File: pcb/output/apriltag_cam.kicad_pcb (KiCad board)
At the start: 4 copper layers, 48 x 48 mm, 152 parts, among them J1 USB-C, J2 JTAG, SW1 BOOTSEL, U1 LFE5U-85F-8BG381C, U10 OV9281, U11 USBLC6-2SC6, U2 RP2350A, U3 W25Q128JVSIQ, U4 TLV62569, U5 TLV62569, U6 TLV75525, U7 TLV75518, U8 TLV75528, U9 TLV75512, Y1 12MHz, Y2 24MHz 1.8V

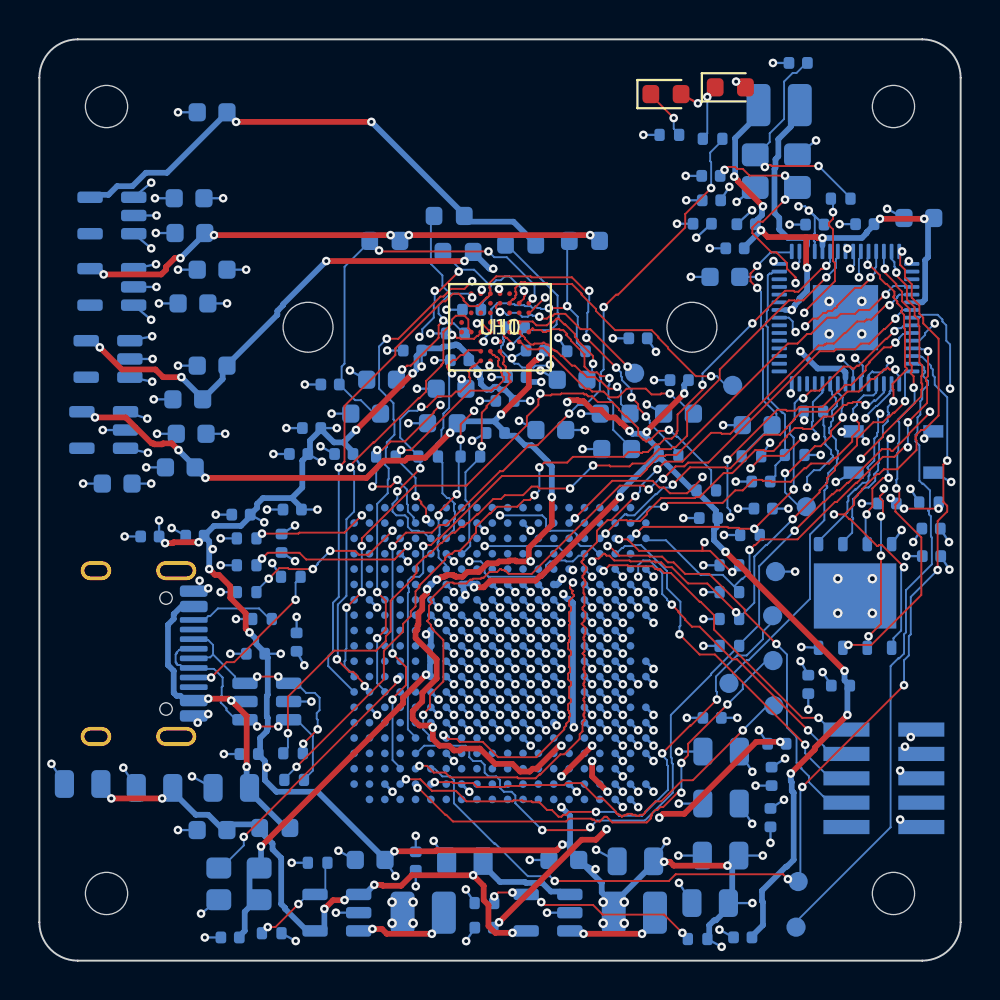
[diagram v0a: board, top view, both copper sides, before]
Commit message: Move status LEDs to the flat part of the housing roof
D1 PWR / D2 STAT moved from (9, 21.5) / (12, 21.5), where the front-cover roof
is the 45 degree cone, to (-21.5, -6.5) / (-21.5, -9.5), where the roof is flat
and the light-pipe bores are perpendicular to it. Resistors R14/R15 moved to
the top side next to the LEDs. Only the LED nets were re-routed; the rest of
the board is untouched. Regenerated gerbers, STEP, renders, DRC, housing STL/STEP.

Co-Authored-By: Claude Sonnet 5.5 <noreply@anthropic.com>
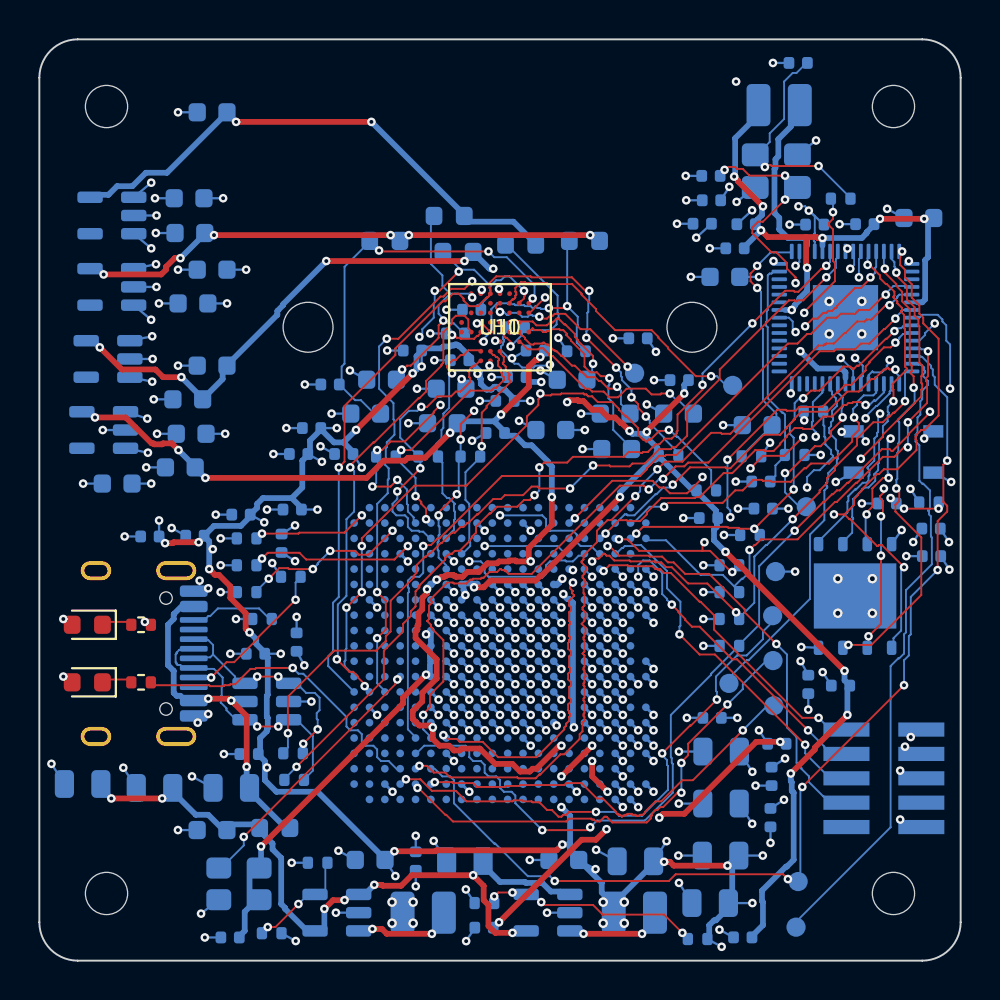
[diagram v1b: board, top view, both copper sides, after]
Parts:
- R14, R15: moved to F.Cu
- moved D2 45.6 mm to (78.5, 109.5), turned to 180 degrees
- moved R15 41.1 mm to (81.3, 109.5)
- moved D1 40.9 mm to (78.5, 106.5), turned to 180 degrees
- moved R14 37.5 mm to (81.3, 106.5), turned to 0 degrees
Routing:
- net LED_STAT: track 42.0 -> 16.1 mm, vias 6 -> 1
- net LED_STAT_K: track 2.37 -> 1.15 mm, vias 1 -> 0
- net LED_PWR_K: track 2.18 -> 1.15 mm, vias 1 -> 0
- net GND: track 170.3 -> 169.6 mm
- net +3V3: track 56.2 -> 55.6 mm, vias 69 -> 70

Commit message: PCB: full re-route for architecture A3 (all 10 frame-bus nets), regenerated outputs, renders and site
pcb/route_sweep.py: grid-router seed sweep on the rebuilt unrouted board, candidate chosen by KiCad DRC (seed 128): 69 violations + 10 unconnected
(85F baseline 72 + 12), all FB_* nets connected. Gerbers, drill, pick-and-place, STEP, 2D/3D renders (render/run_all.sh), bom.csv, BOM page and site rebuilt.
Docs: hardware.md, README, costdown status updated.

Co-Authored-By: Claude Sonnet 5.5 <noreply@anthropic.com>
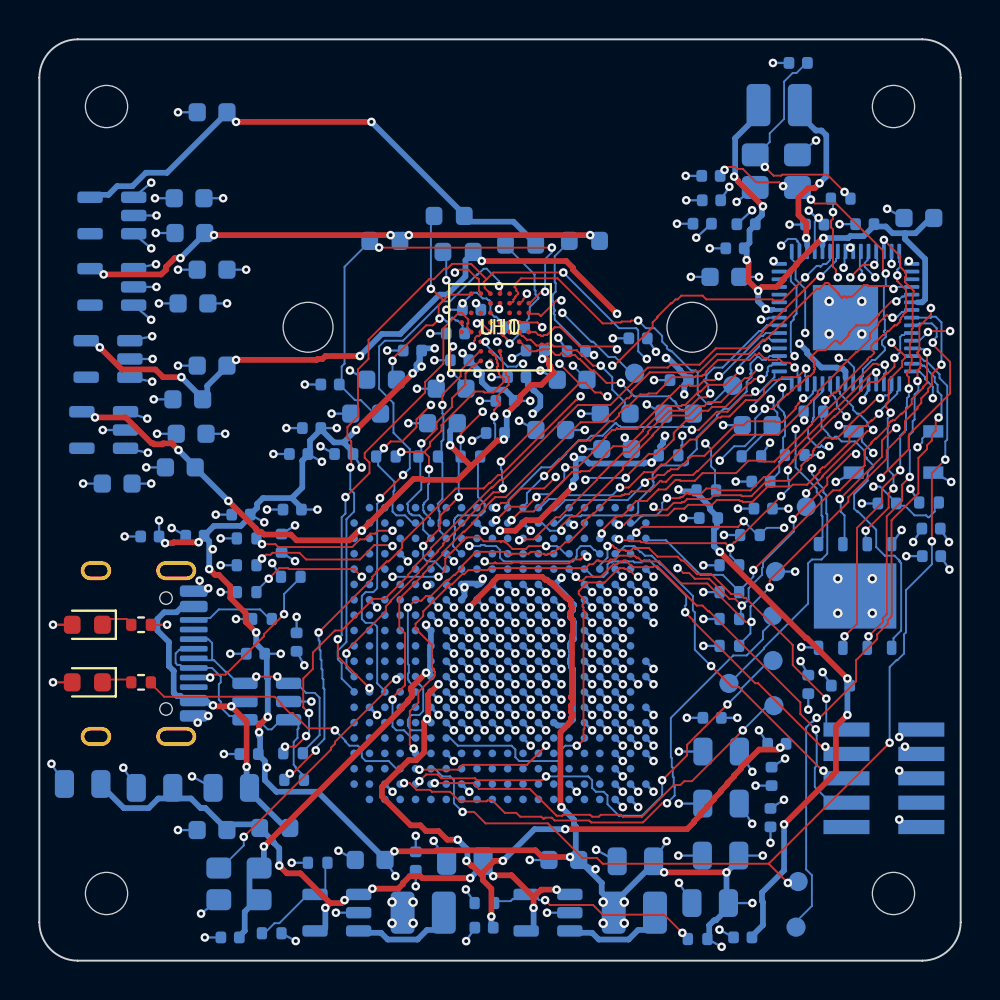
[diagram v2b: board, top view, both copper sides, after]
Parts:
- U1: value LFE5U-85F-8BG381C -> LFE5U-45F-8BG381C
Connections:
- U1 pad K1: (no net) -> FB_D4
- U1 pad K2: (no net) -> FB_CLK
- U1 pad L1: (no net) -> FB_D3
- U1 pad L2: (no net) -> FB_D7
- U1 pad M1: (no net) -> FB_D2
- U1 pad M3: (no net) -> FB_FS
- U1 pad N1: (no net) -> FB_D1
- U1 pad N2: (no net) -> FB_D6
- U1 pad P1: (no net) -> FB_D0
- U1 pad P2: (no net) -> FB_D5
- U2 pad 27: (no net) -> FB_D0
- U2 pad 28: (no net) -> FB_D1
- U2 pad 29: (no net) -> FB_D2
- U2 pad 31: (no net) -> FB_D3
- U2 pad 32: (no net) -> FB_D4
- U2 pad 33: (no net) -> FB_D5
- U2 pad 34: (no net) -> FB_D6
- U2 pad 35: (no net) -> FB_D7
- U2 pad 36: (no net) -> FB_CLK
- U2 pad 37: (no net) -> FB_FS
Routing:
- net FB_CLK: track 0.00 -> 19.1 mm, vias 0 -> 4
- net FB_FS: track 0.00 -> 19.0 mm, vias 0 -> 2
- net FB_D2: track 0.00 -> 18.8 mm, vias 0 -> 2
- net FB_D4: track 0.00 -> 18.2 mm, vias 0 -> 5
- net FB_D7: track 0.00 -> 18.1 mm, vias 0 -> 2
- net FB_D1: track 0.00 -> 17.5 mm, vias 0 -> 2
- net FB_D3: track 0.00 -> 17.4 mm, vias 0 -> 2
- net FB_D5: track 0.00 -> 17.3 mm
- net FB_D6: track 0.00 -> 16.9 mm, vias 0 -> 3
- net FB_D0: track 0.00 -> 16.2 mm, vias 0 -> 2
- net +2V5: track 88.0 -> 99.2 mm, vias 20 -> 18
- net QSPI_SS: track 33.1 -> 26.0 mm, vias 4 -> 2
- net GND: track 169.6 -> 175.4 mm, vias 235 -> 236
- net +1V8: track 109.7 -> 113.7 mm, vias 20 -> 24
- net FPGA_PROGRAMN: track 22.0 -> 25.8 mm
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
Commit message: PCB production readiness: fix floating +3V3/GND pad clusters, in-stock LDOs, flash label, crystal check, 1.9 mm holder holes, ERC tests
KiCad DRC unconnected items were real (RP2350 IOVDD pads 20/11, FPGA VCCIO balls, decoupling caps): linked with pcb/fix_power_links.py.
U6/U8 now ME6211C25M5G-N / ME6211C28M5G-N (in stock), flash label W25Q128JVPIQ, crystal load 10.5 pF vs 10 pF documented,
lens holder screw holes 2.6 -> 1.9 mm. DRC: 0 unconnected, no clearance errors. New tests/test_pcb_erc.py.

Co-Authored-By: Claude Sonnet 5.5 <noreply@anthropic.com>
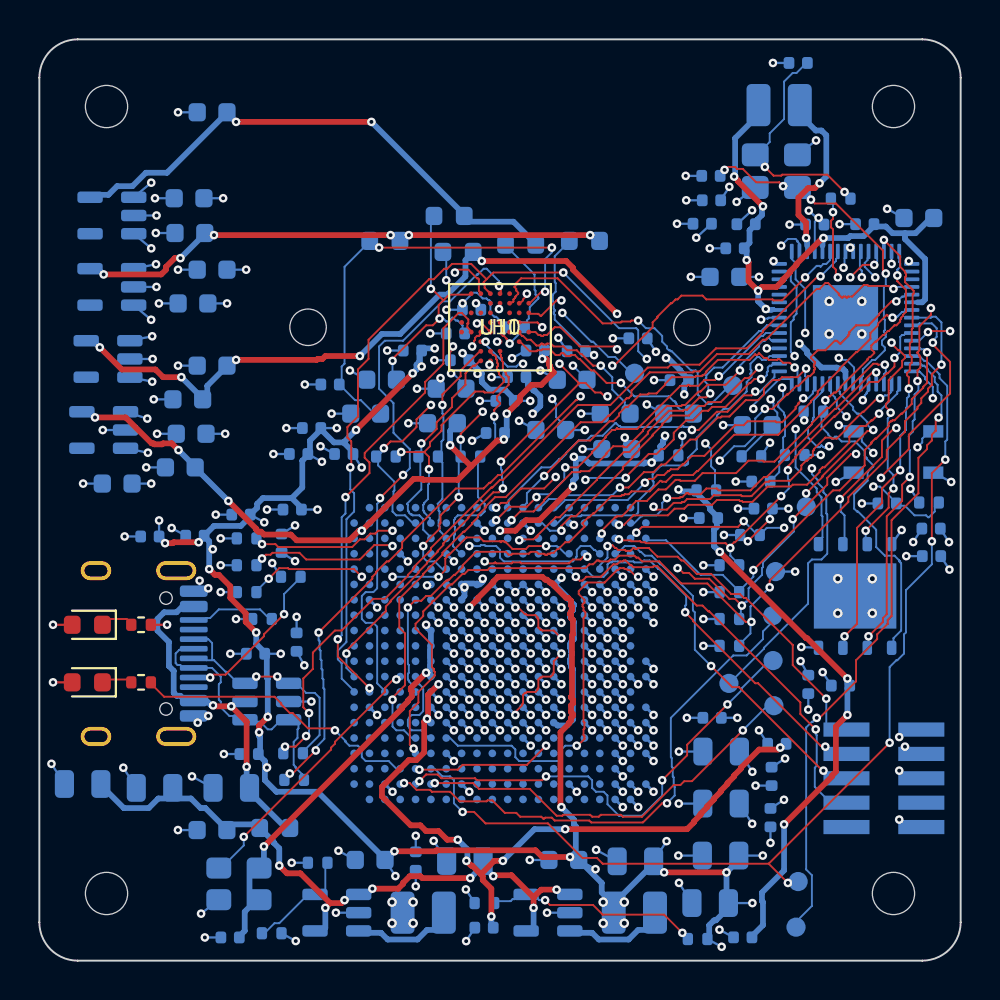
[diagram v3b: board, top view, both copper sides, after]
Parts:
- U3: value W25Q128JVSIQ -> W25Q128JVPIQ
- U6: value TLV75525 -> ME6211C25
- U8: value TLV75528 -> ME6211C28
- Y1: value 12MHz -> 12MHz 10pF
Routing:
- net +3V3: track 57.4 -> 108.6 mm, vias 70 -> 73
- net QSPI_SD0: track 17.5 -> 20.4 mm
- net GND: track 175.4 -> 178.0 mm
